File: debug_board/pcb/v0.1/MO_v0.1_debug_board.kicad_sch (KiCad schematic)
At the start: 32 parts, among them j1 DAC_PWR, j10 nRF_PWR, j11 U0_TX, j12 nRF_VBUS, j13 SWDIO, j14 SWDCLK, j15 U0_RX, j16 nRF_DCCH, j2 SD_nFLAG, j3 DAC_nFLAG, j4 nRF_RESET, j5 FW_PWR_FAULT, j6 SD_PWR, j7 3v3_PI, j8 3v3_LDO, j9 GND

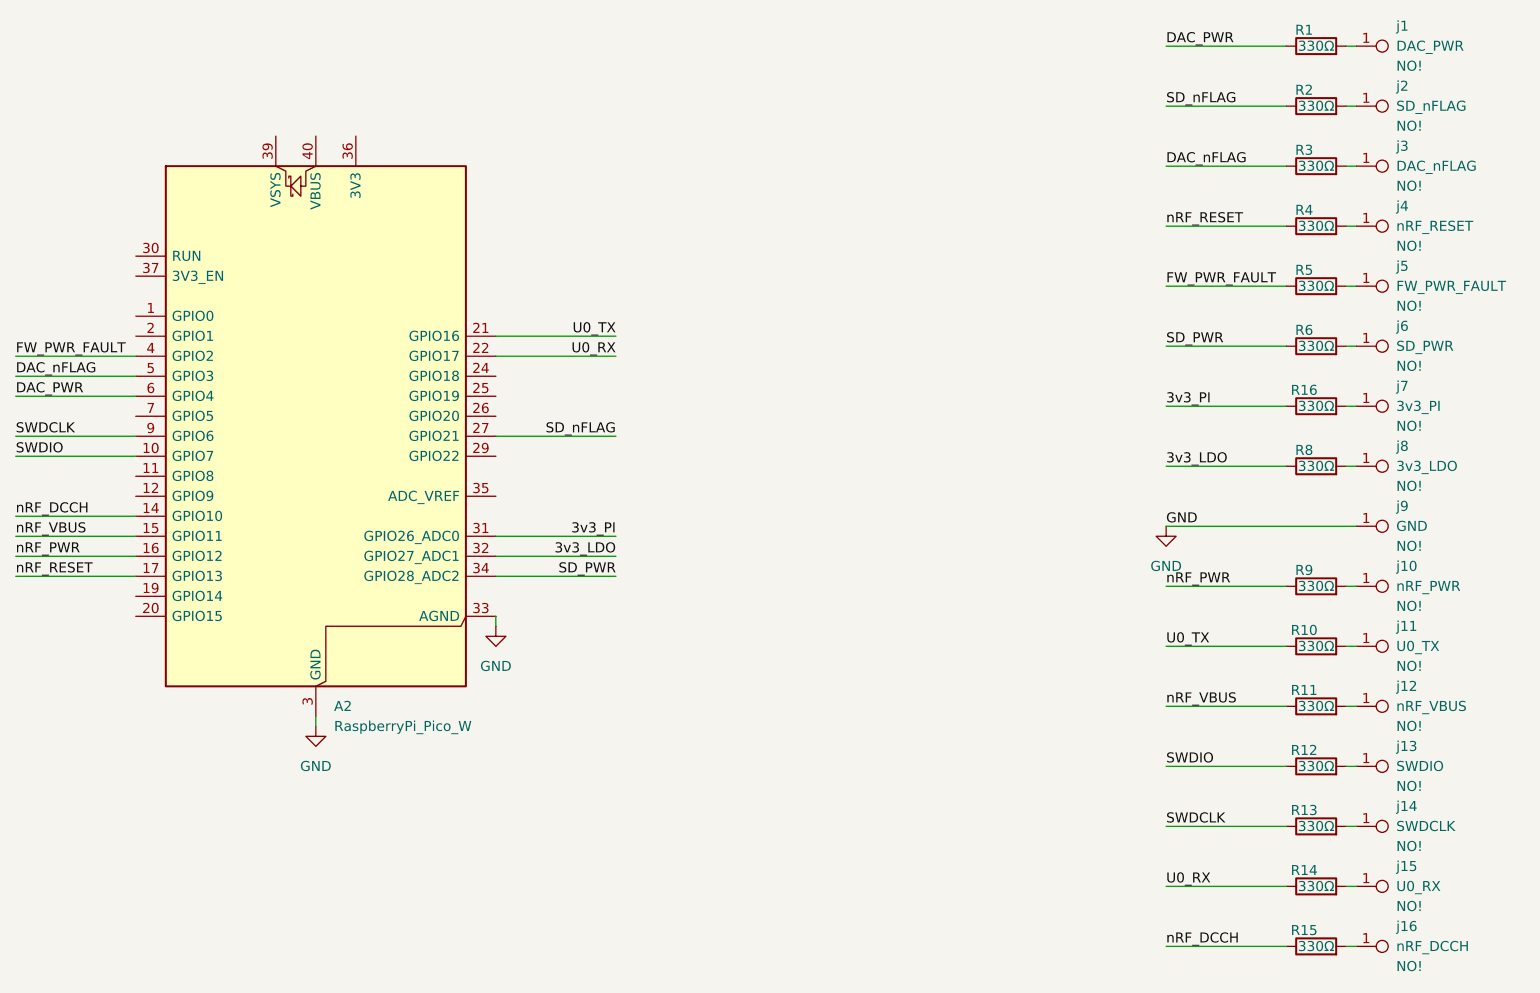
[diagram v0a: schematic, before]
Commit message: Update debug board to use pi zero instead of pico
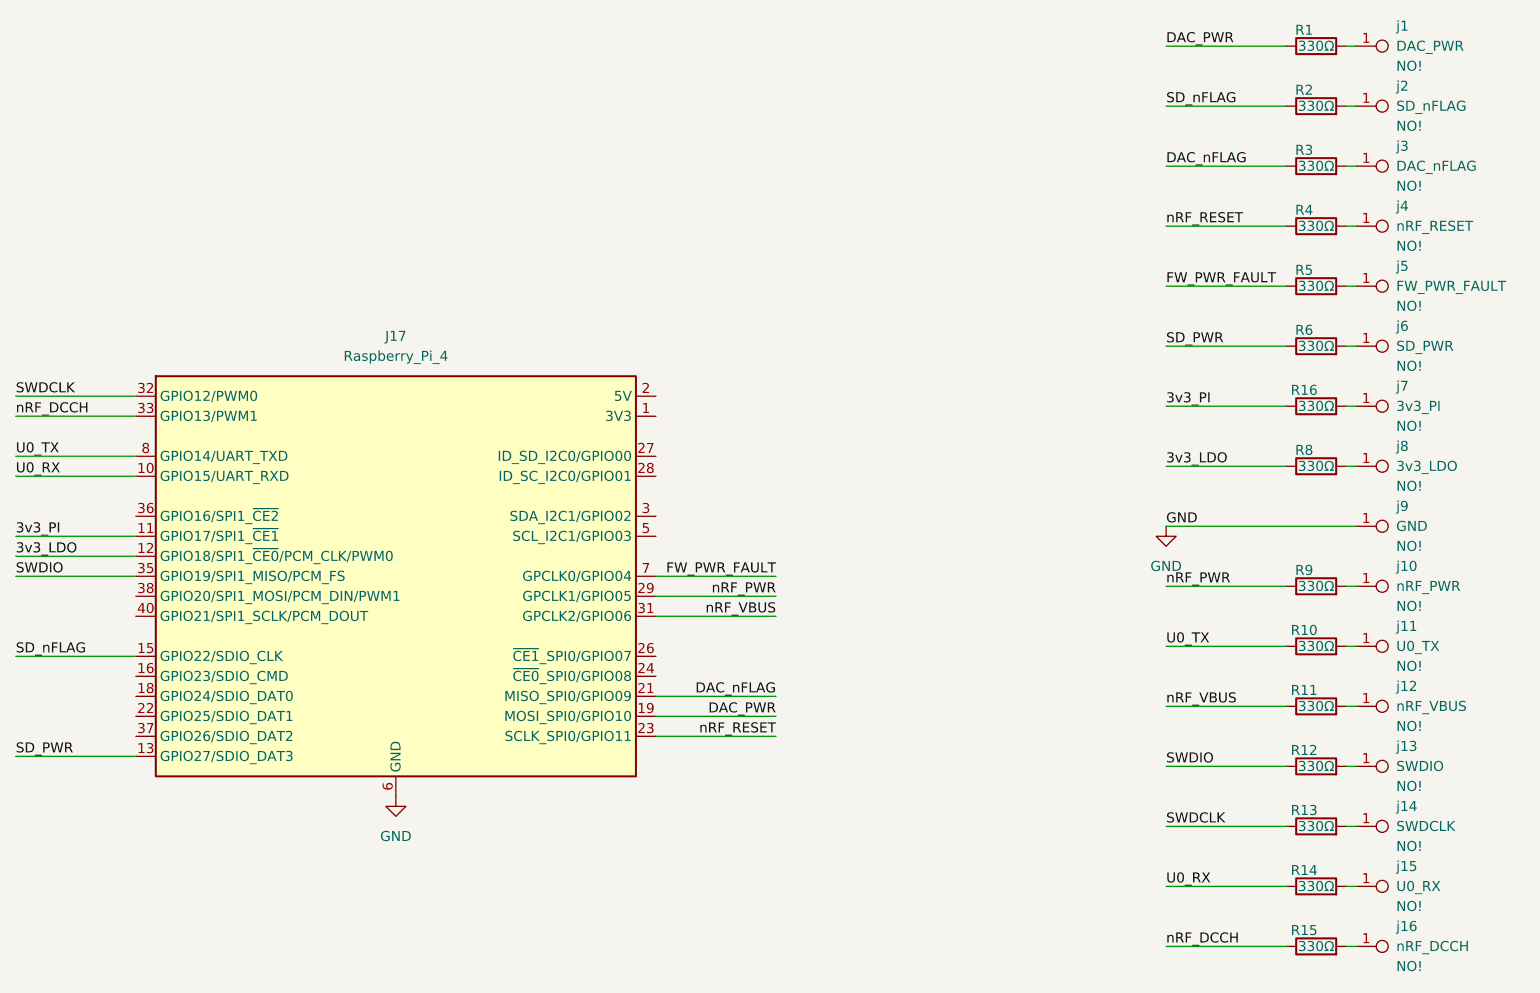
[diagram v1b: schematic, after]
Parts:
- removed A2: RaspberryPi_Pico_W, Module:RaspberryPi_Pico_W_SMD_HandSolder, symbol MCU_Module:RaspberryPi_Pico_W
- added J17: Raspberry_Pi_4, Connector_PinSocket_2.54mm:PinSocket_2x20_P2.54mm_Vertical, symbol Connector:Raspberry_Pi_4
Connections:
- net 3v3_LDO: now also J17.12 (GPIO18/SPI1_~{CE0}/PCM_CLK/PWM0)
- net 3v3_PI: now also J17.11 (GPIO17/SPI1_~{CE1})
- net DAC_PWR: now also J17.19 (MOSI_SPI0/GPIO10)
- net DAC_nFLAG: now also J17.21 (MISO_SPI0/GPIO09)
- net FW_PWR_FAULT: now also J17.7 (GPCLK0/GPIO04)
- net GND: now also J17.14 (GND), J17.20 (GND), J17.25 (GND), J17.30 (GND), J17.34 (GND), J17.39 (GND), J17.6 (GND), J17.9 (GND)
- net SD_PWR: now also J17.13 (GPIO27/SDIO_DAT3)
- net SD_nFLAG: now also J17.15 (GPIO22/SDIO_CLK)
- net SWDCLK: now also J17.32 (GPIO12/PWM0)
- net SWDIO: now also J17.35 (GPIO19/SPI1_MISO/PCM_FS)
- net U0_RX: now also J17.10 (GPIO15/UART_RXD)
- net U0_TX: now also J17.8 (GPIO14/UART_TXD)
- net nRF_DCCH: now also J17.33 (GPIO13/PWM1)
- net nRF_PWR: now also J17.29 (GPCLK1/GPIO05)
- net nRF_RESET: now also J17.23 (SCLK_SPI0/GPIO11)
- net nRF_VBUS: now also J17.31 (GPCLK2/GPIO06)
- new net: J17.1 (3V3), J17.17 (3V3)
- new net: J17.2 (5V), J17.4 (5V)
